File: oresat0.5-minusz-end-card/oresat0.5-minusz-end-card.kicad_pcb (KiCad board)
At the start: 4 copper layers, 99.8 x 94.6 mm, 36 parts, among them J1 J-SAMTEC-TFM-120-01-L-D-RA, J2 U.FL-R-SMT-1, J3 Harwin M55-7101242R, J4 L-Band Feed, J5 Harwin M55-7101242R, J6 UHF Feed

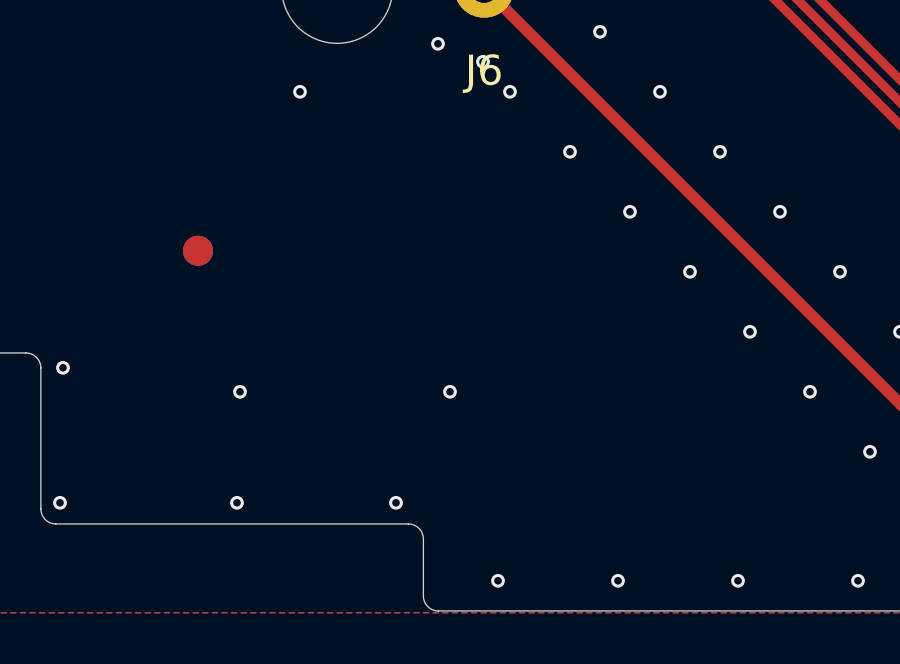
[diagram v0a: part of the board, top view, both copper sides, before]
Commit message: CAM file changes for end card PCBs.
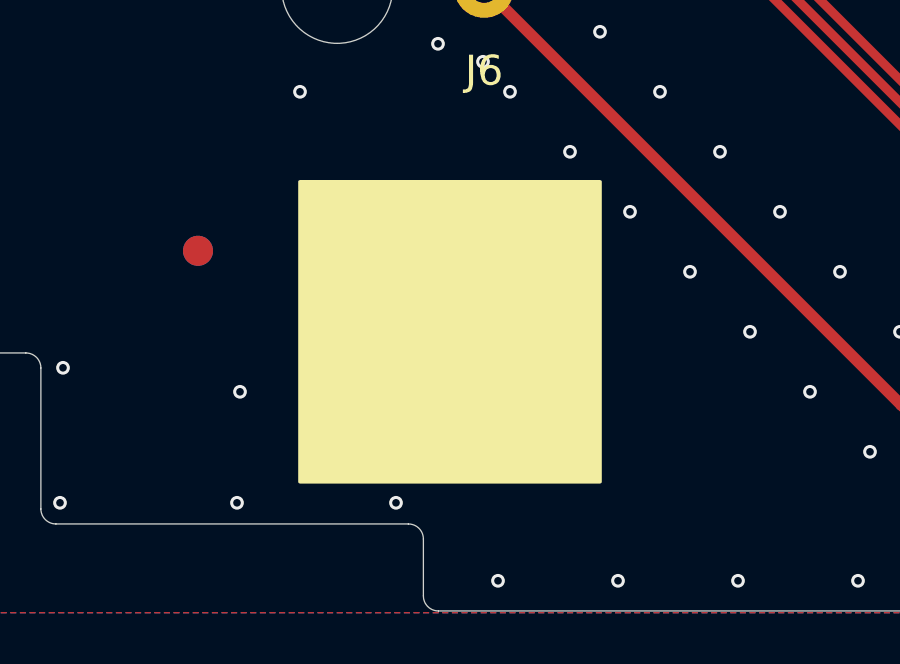
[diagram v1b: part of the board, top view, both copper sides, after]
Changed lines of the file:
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@@
     (fp_arc (start 82.81 -86.4) (mid 82.456447 -86.546447) (end 82.31 -86.9) (layer "Cmts.User") (width 0.001))
     (fp_arc (start 91.13205 -94.6) (mid 90.399999 -93.86795) (end 89.4 -93.599999) (layer "Cmts.User") (width 0.001))
-    (fp_arc (start 68.63205 -90.6) (mid 68.278529 -90.746464) (end 68.13205 -91.1) (layer "Cmts.User") (width 0.001))
+    (fp_arc (start 68.63205 -90.6) (mid 68.278494 -90.746458) (end 68.13205 -91.1) (layer "Cmts.User") (width 0.001))
     (fp_arc (start 73.49 -86.9) (mid 73.343553 -86.546447) (end 72.99 -86.4) (layer "Cmts.User") (width 0.001))
     (fp_arc (start 85.49 -86.9) (mid 85.343553 -86.546447) (end 84.99 -86.4) (layer "Cmts.User") (width 0.001))
@@
     (fp_arc (start 70.81 -86.4) (mid 70.456447 -86.546447) (end 70.31 -86.9) (layer "Cmts.User") (width 0.001))
     (fp_arc (start 97.05 -8.1) (mid 97.196447 -8.453553) (end 97.55 -8.6) (layer "Cmts.User") (width 0.001))
-    (fp_arc (start 87.66795 -91.1) (mid 87.521506 -90.746429) (end 87.16795 -90.6) (layer "Cmts.User") (width 0.001))
+    (fp_arc (start 87.66795 -91.1) (mid 87.5215 -90.746464) (end 87.16795 -90.6) (layer "Cmts.User") (width 0.001))
     (fp_arc (start 3.25 -2.9) (mid 2.896447 -3.046447) (end 2.75 -3.4) (layer "Cmts.User") (width 0.001))
     (fp_arc (start 16 0) (mid 15.646447 -0.146447) (end 15.5 -0.5) (layer "Cmts.User") (width 0.001))
@@
     (fp_arc (start 2.25 -8.6) (mid 2.603553 -8.453553) (end 2.75 -8.1) (layer "Cmts.User") (width 0.001))
     (fp_arc (start 66.4 -93.6) (mid 65.400001 -93.867949) (end 64.66795 -94.599999) (layer "Cmts.User") (width 0.001))
-    (fp_arc (start 87.66795 -93.1) (mid 87.814394 -93.453571) (end 88.16795 -93.6) (layer "Cmts.User") (width 0.001))
-    (fp_arc (start 67.63205 -93.6) (mid 67.985571 -93.453536) (end 68.13205 -93.1) (layer "Cmts.User") (width 0.001))
+    (fp_arc (start 87.66795 -93.1) (mid 87.8144 -93.453536) (end 88.16795 -93.6) (layer "Cmts.User") (width 0.001))
+    (fp_arc (start 67.63205 -93.6) (mid 67.985606 -93.453542) (end 68.13205 -93.1) (layer "Cmts.User") (width 0.001))
     (fp_circle (center 70.31 -86.4) (end 70.47 -86.4) (layer "Cmts.User") (width 0.001) (fill none))
     (fp_circle (center 85.49 -86.4) (end 85.65 -86.4) (layer "Cmts.User") (width 0.001) (fill none))
@@
       (net 2 "GND") (pintype "passive") (solder_mask_margin 0.0635))
   )
+  (gr_rect (start 110 138) (end 120 148) (layer "F.SilkS") (width 0.12) (fill solid))
   (gr_poly
     (pts

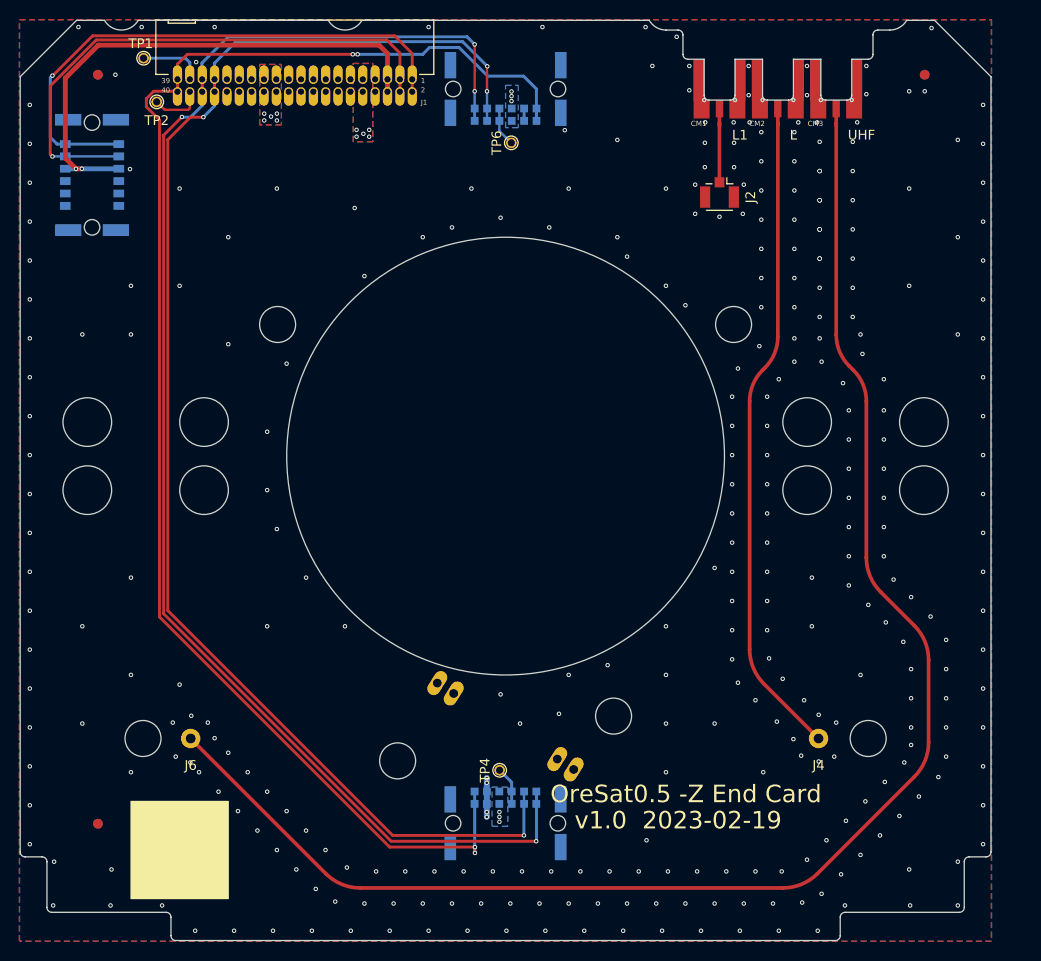
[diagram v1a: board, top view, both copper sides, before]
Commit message: Updated OreSat 0.5 end card board outlines and mounting holes, and fixed KiCad library warnings
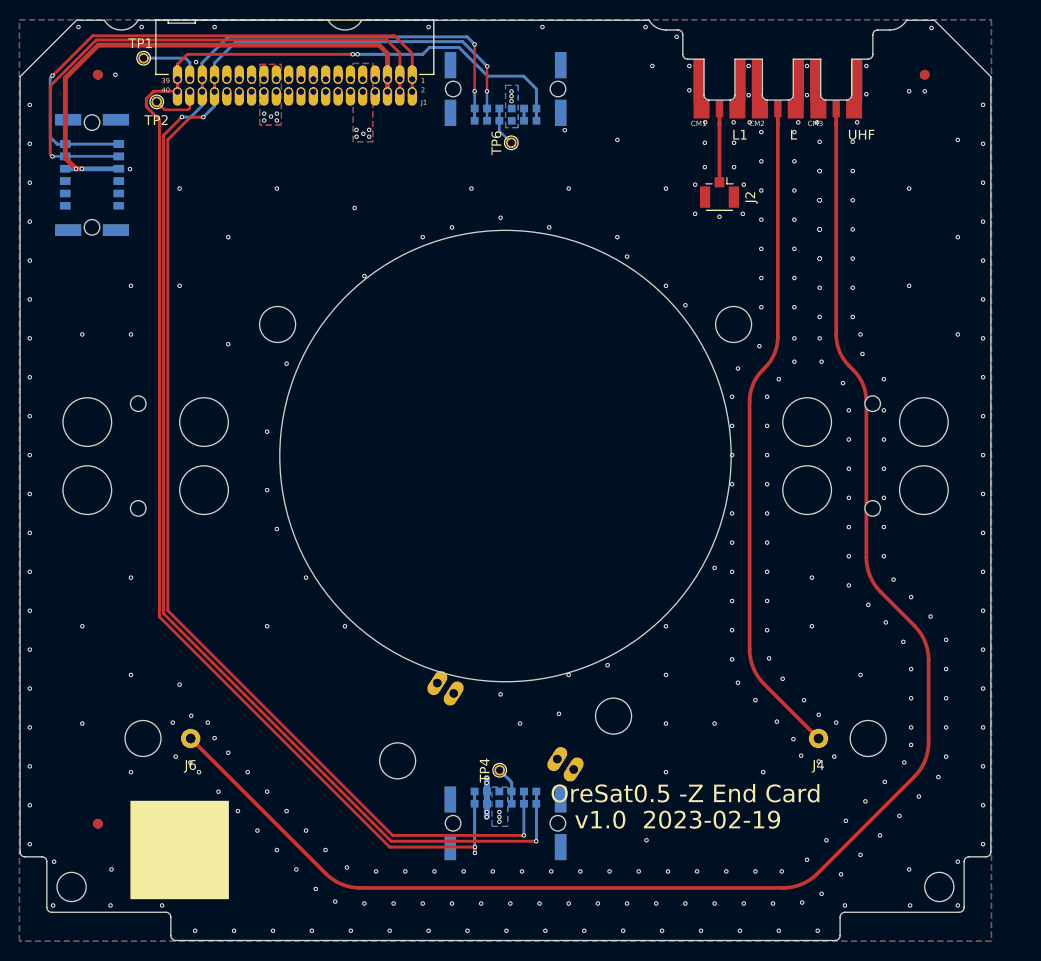
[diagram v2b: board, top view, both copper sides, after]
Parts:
- added REF**: Hole-1.6mm-NPTH, oresat-misc:Hole-1.6mm-NPTH, F.Cu at (110.8, 97.1)
- added REF**: Hole-1.6mm-NPTH, oresat-misc:Hole-1.6mm-NPTH, F.Cu at (186.2, 97.1)
- added REF**: Hole-1.6mm-NPTH, oresat-misc:Hole-1.6mm-NPTH, F.Cu at (110.8, 107.9)
- added REF**: Hole-1.6mm-NPTH, oresat-misc:Hole-1.6mm-NPTH, F.Cu at (186.2, 107.9)
- PCB1: footprint plusz-end-card-with-turnstile:ORESAT-CARD-V1.3-GENERIC-3RF -> oresat-pcbs:ORESAT-CARD-V1.3-3RF
- moved PCB1 70.5 mm to (148.5, 102.5)
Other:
- outline, holes or cut-outs redrawn

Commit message: Updated -Z end card and DXF
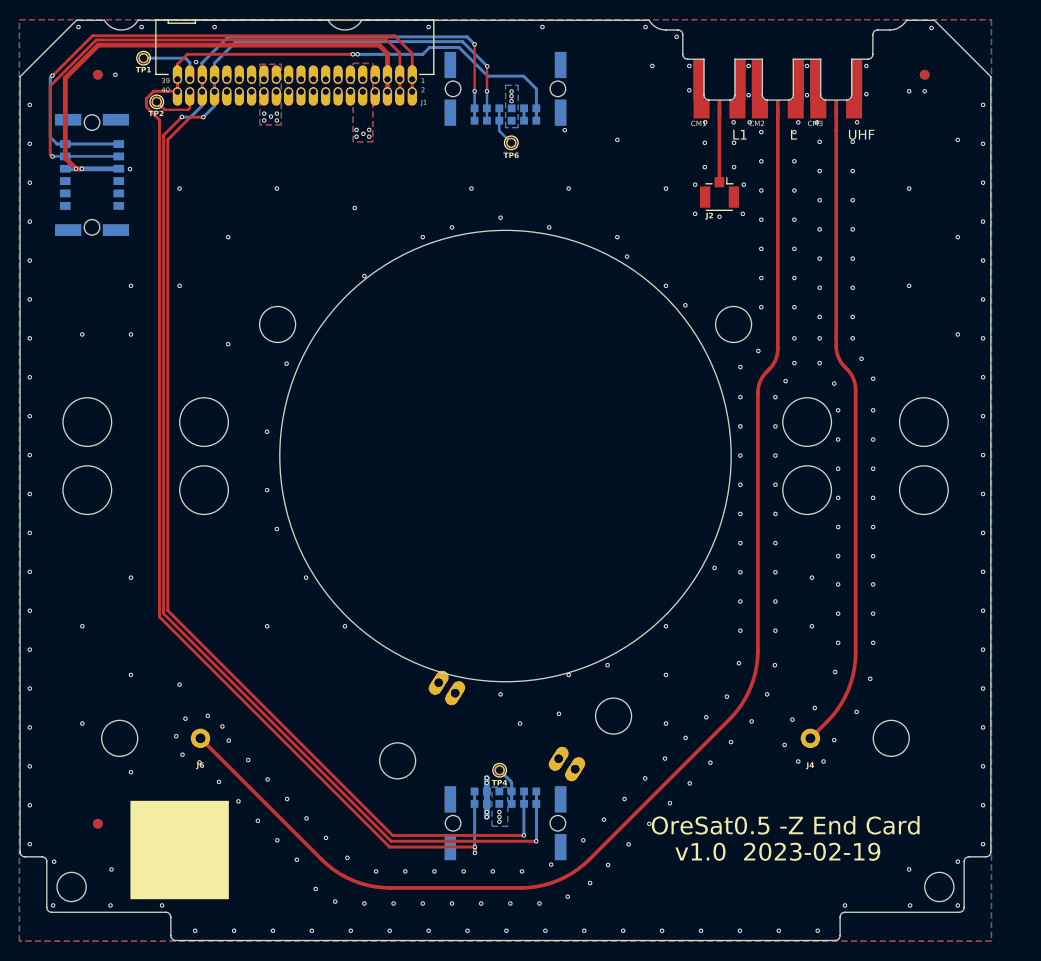
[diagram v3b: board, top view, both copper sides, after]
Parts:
- removed the REF** at (110.8, 97.1)
- removed the REF** at (186.2, 97.1)
- removed the REF** at (110.8, 107.9)
- removed the REF** at (186.2, 107.9)
- CM1, CM2, CM3: footprint oresat-connectors:J-MOLEX-SMPM-073300-003X -> oresat-connectors:J-MOLEX-SMPM-073300-002X
- J1: footprint oresat-footprints:J-SAMTEC-TFM-120-X1-XXX-D-RA -> oresat-connectors:J-SAMTEC-TFM-120-X1-XXX-D-RA
- J4: value L-Band Feed -> UHF Feed
- J6: value UHF Feed -> L-Band Feed
- TP1, TP2, TP4, TP6: footprint oresat-misc:TestPoint-MinTH -> oresat-misc:TestPoint-0.75mm-th
- moved HW4 2.40 mm to (108.8, 131.5)
- moved HW1 2.37 mm to (188.2, 131.5)
- moved J6 1.01 mm to (117.2, 131.5)
- moved J4 0.84 mm to (179.8, 131.5)
- moved R1 0.15 mm to (148.7, 130.2)
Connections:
- J4 pad 1: /L BAND/LBAND -> /UHF/UHF
- J6 pad 1: /UHF/UHF -> /L BAND/LBAND
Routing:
- net /UHF/UHF: track 155.5 -> 66.7 mm
- net /L BAND/LBAND: track 66.6 -> 131.0 mm
- net /L1 BAND/L1BAND: track 5.93 -> 7.55 mm
- net GND: vias 335 -> 300
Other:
- board text removed: "The exact position of this connector needs to be checked once we have the DXF"

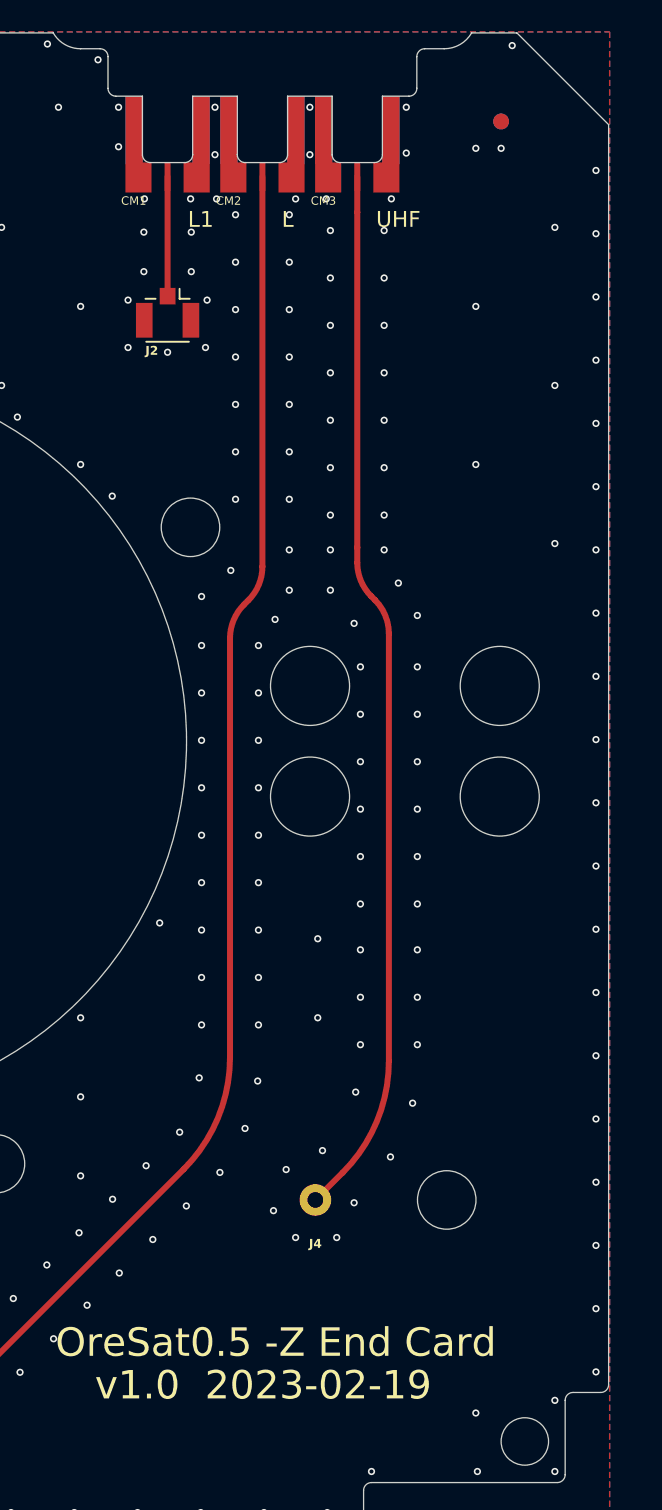
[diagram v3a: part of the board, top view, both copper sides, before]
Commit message: Updated -Z end card date/version number on silkscreen
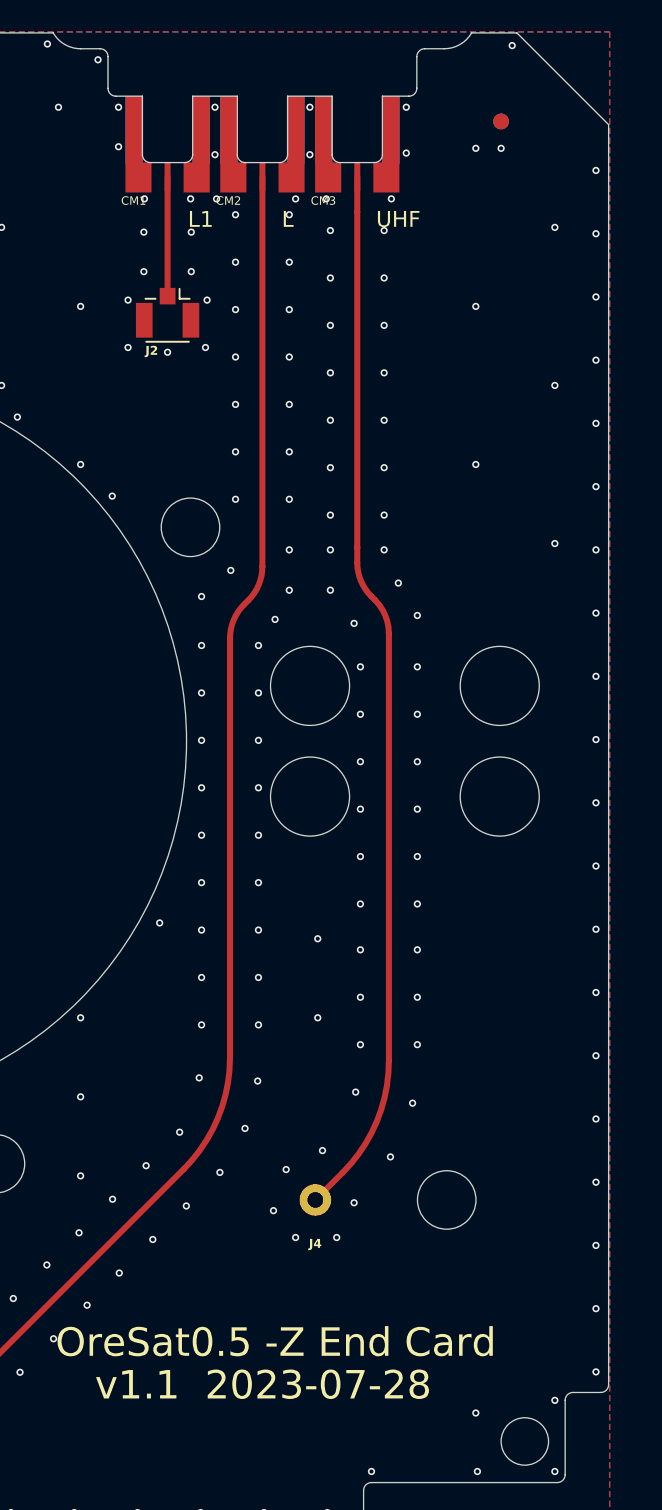
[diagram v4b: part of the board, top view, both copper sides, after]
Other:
- board text added: "v1.1 2023-07-28"
- board text removed: "v1.0 2023-02-19"
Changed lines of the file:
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@@
     (fp_arc (start 16.5 -43.8) (mid 15.500001 -44.067949) (end 14.76795 -44.799999)
       (stroke (width 0.001) (type solid)) (layer "Dwgs.User"))
-    (fp_arc (start 17.73205 -43.8) (mid 18.085571 -43.653536) (end 18.23205 -43.3)
+    (fp_arc (start 17.73205 -43.8) (mid 18.085606 -43.653542) (end 18.23205 -43.3)
       (stroke (width 0.001) (type solid)) (layer "Dwgs.User"))
-    (fp_arc (start 18.73205 -40.8) (mid 18.378529 -40.946464) (end 18.23205 -41.3)
+    (fp_arc (start 18.73205 -40.8) (mid 18.378494 -40.946458) (end 18.23205 -41.3)
       (stroke (width 0.001) (type solid)) (layer "Dwgs.User"))
     (fp_arc (start 20.91 -36.6) (mid 20.556447 -36.746447) (end 20.41 -37.1)
@@
     (fp_arc (start 35.59 -37.1) (mid 35.443553 -36.746447) (end 35.09 -36.6)
       (stroke (width 0.001) (type solid)) (layer "Dwgs.User"))
-    (fp_arc (start 37.76795 -43.3) (mid 37.914394 -43.653571) (end 38.26795 -43.8)
+    (fp_arc (start 37.76795 -43.3) (mid 37.9144 -43.653536) (end 38.26795 -43.8)
       (stroke (width 0.001) (type solid)) (layer "Dwgs.User"))
-    (fp_arc (start 37.76795 -41.3) (mid 37.621506 -40.946429) (end 37.26795 -40.8)
+    (fp_arc (start 37.76795 -41.3) (mid 37.6215 -40.946464) (end 37.26795 -40.8)
       (stroke (width 0.001) (type solid)) (layer "Dwgs.User"))
     (fp_arc (start 41.23205 -44.8) (mid 40.499999 -44.06795) (end 39.5 -43.799999)
@@
     (fp_arc (start 16.499999 -43.8) (mid 15.5 -44.067949) (end 14.76795 -44.8)
       (stroke (width 0.001) (type solid)) (layer "Edge.Cuts"))
-    (fp_arc (start 17.73205 -43.8) (mid 18.085571 -43.653536) (end 18.23205 -43.3)
+    (fp_arc (start 17.73205 -43.8) (mid 18.085606 -43.653542) (end 18.23205 -43.3)
       (stroke (width 0.001) (type solid)) (layer "Edge.Cuts"))
-    (fp_arc (start 18.73205 -40.8) (mid 18.378529 -40.946464) (end 18.23205 -41.3)
+    (fp_arc (start 18.73205 -40.8) (mid 18.378494 -40.946458) (end 18.23205 -41.3)
       (stroke (width 0.001) (type solid)) (layer "Edge.Cuts"))
     (fp_arc (start 20.91 -36.6) (mid 20.556447 -36.746447) (end 20.41 -37.1)
@@
     (fp_arc (start 35.59 -37.1) (mid 35.443553 -36.746447) (end 35.09 -36.6)
       (stroke (width 0.001) (type solid)) (layer "Edge.Cuts"))
-    (fp_arc (start 37.76795 -43.3) (mid 37.914394 -43.653571) (end 38.26795 -43.8)
+    (fp_arc (start 37.76795 -43.3) (mid 37.9144 -43.653536) (end 38.26795 -43.8)
       (stroke (width 0.001) (type solid)) (layer "Edge.Cuts"))
-    (fp_arc (start 37.76795 -41.3) (mid 37.621506 -40.946429) (end 37.26795 -40.8)
+    (fp_arc (start 37.76795 -41.3) (mid 37.6215 -40.946464) (end 37.26795 -40.8)
       (stroke (width 0.001) (type solid)) (layer "Edge.Cuts"))
     (fp_arc (start 41.232049 -44.8) (mid 40.499999 -44.06795) (end 39.5 -43.8)
@@
   (gr_curve (pts (xy 172.117721 115.708568) (xy 171.747625 115.922243) (xy 171.747625 116.349593) (xy 171.747625 116.349593))
     (stroke (width 0.01) (type solid)) (layer "User.1"))
-  (gr_text "v1.0  2023-02-19" (at 165.9 144.3) (layer "F.SilkS")
+  (gr_text "v1.1  2023-07-28" (at 165.9 144.3) (layer "F.SilkS")
     (effects (font (size 1.8 1.8) (thickness 0.2)) (justify left bottom))
   )
